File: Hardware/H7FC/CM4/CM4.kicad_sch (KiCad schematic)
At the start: 0 parts

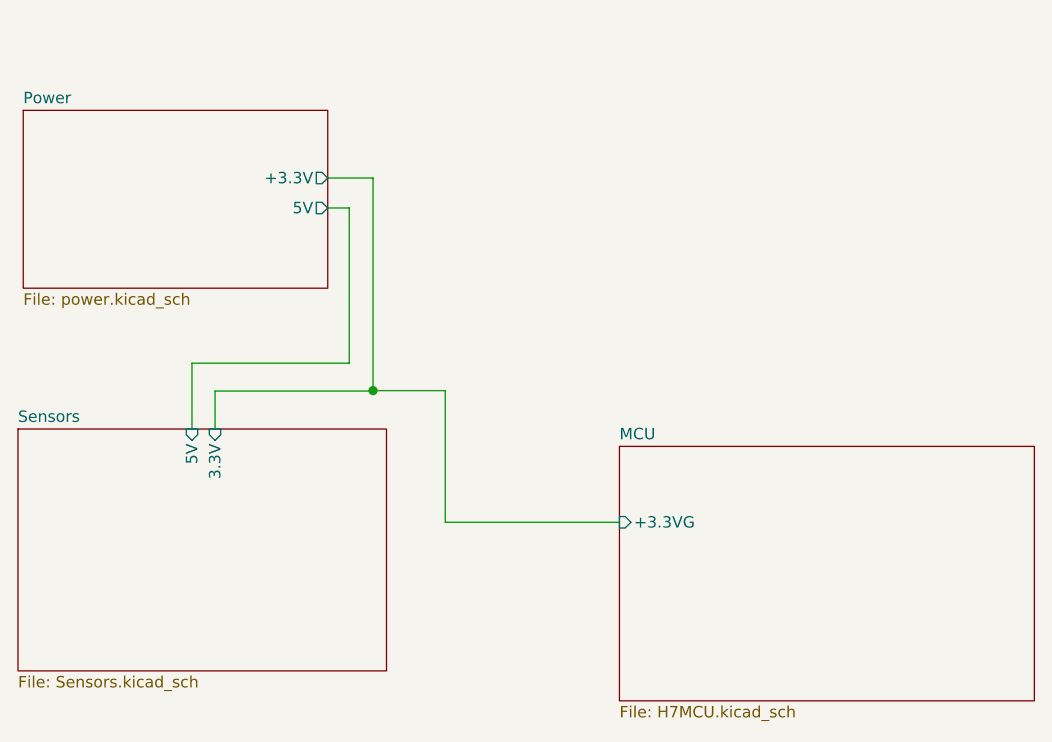
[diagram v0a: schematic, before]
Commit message: Set initial cUbeMX Cconfig. Fixed Clock and GPIO bug
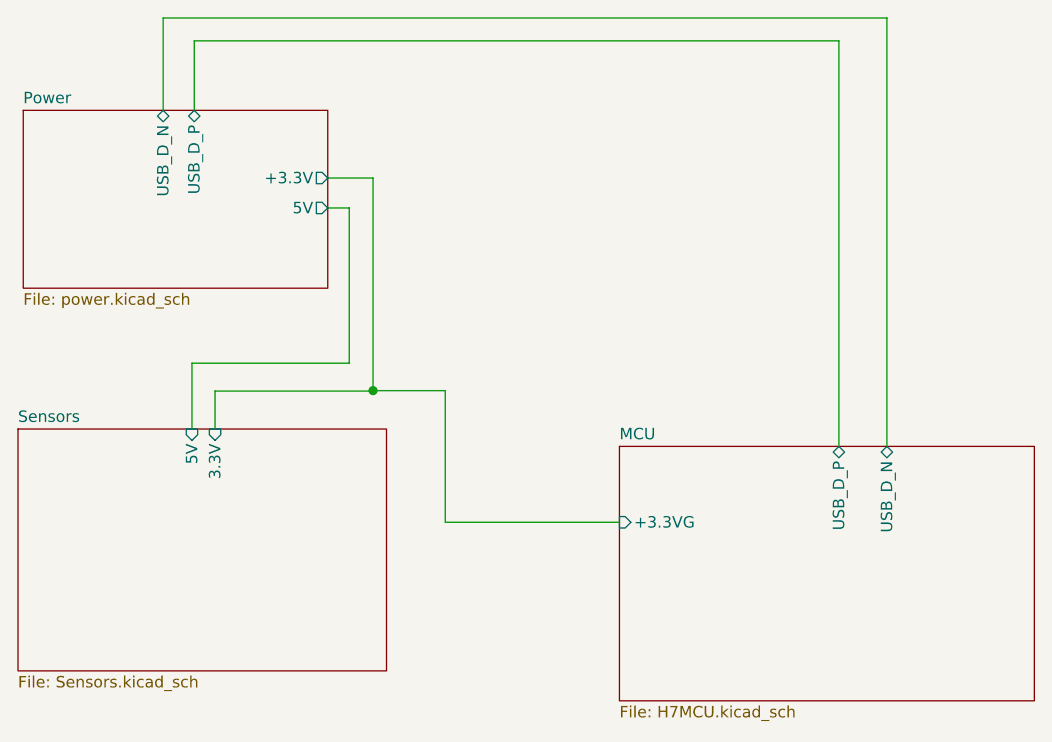
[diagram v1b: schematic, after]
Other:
- sheet MCU ports: added USB_D_N, USB_D_P; removed none
- sheet Power ports: added USB_D_N, USB_D_P; removed none
